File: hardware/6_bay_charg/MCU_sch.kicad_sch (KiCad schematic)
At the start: 21 parts, among them J2 Conn_ARM_SWD_TagConnect_TC203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, Q1 2N7002, U4 TCA9548APWR, U5 STM32L031K6Tx

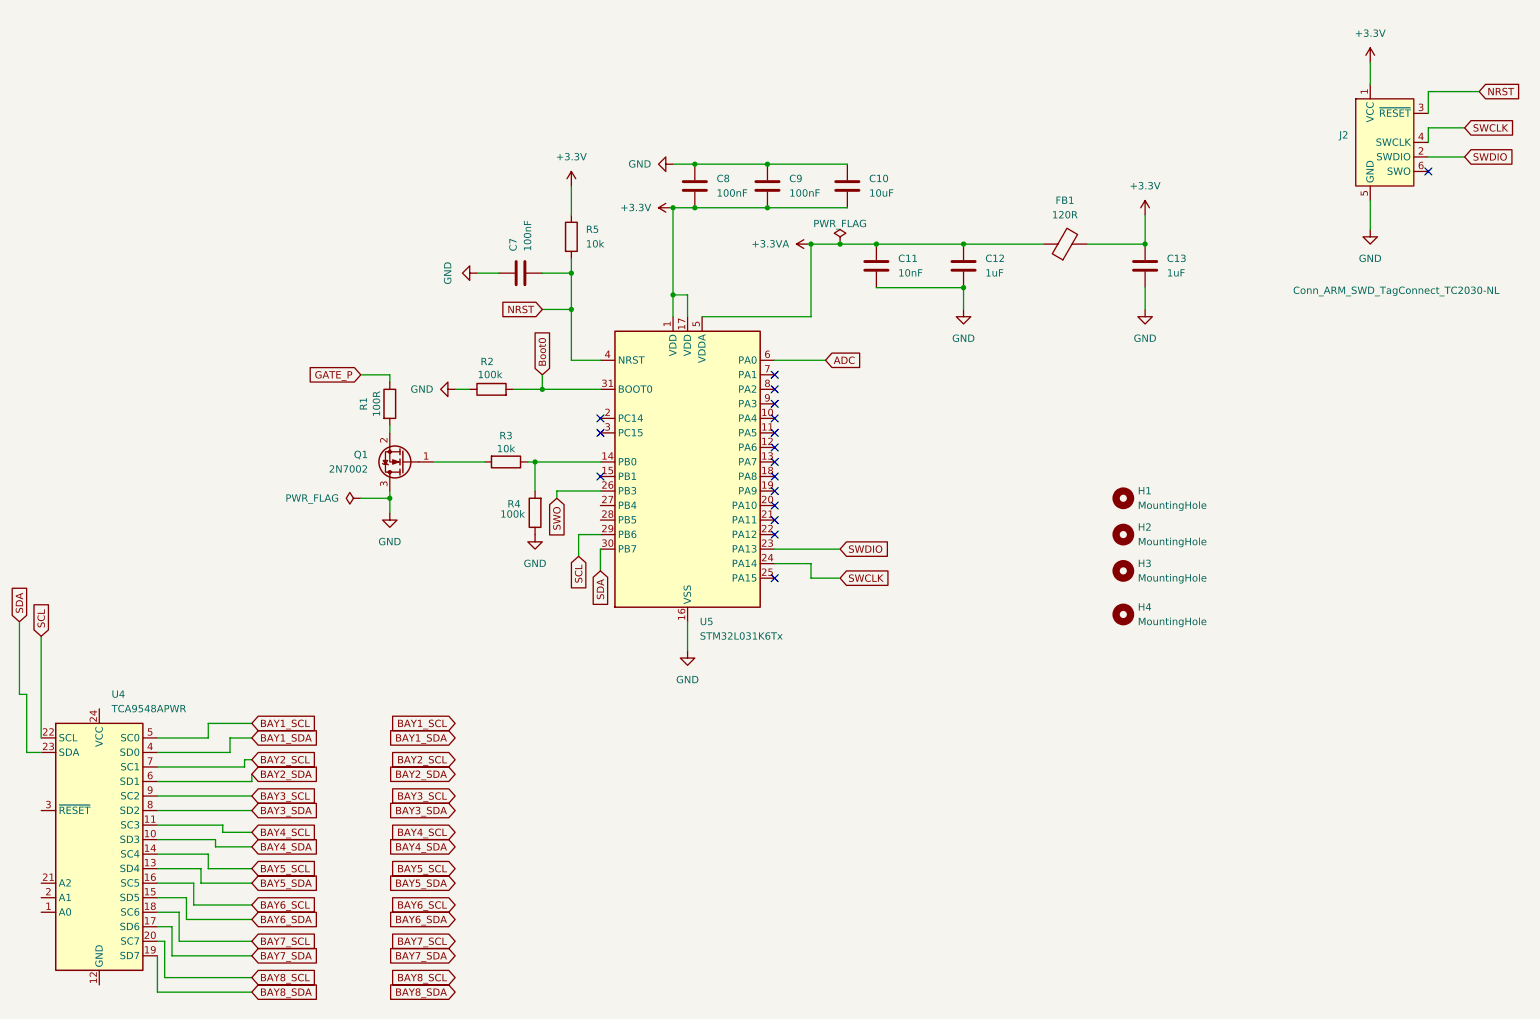
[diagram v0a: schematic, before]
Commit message: adding 3.3v buck sch + bay1
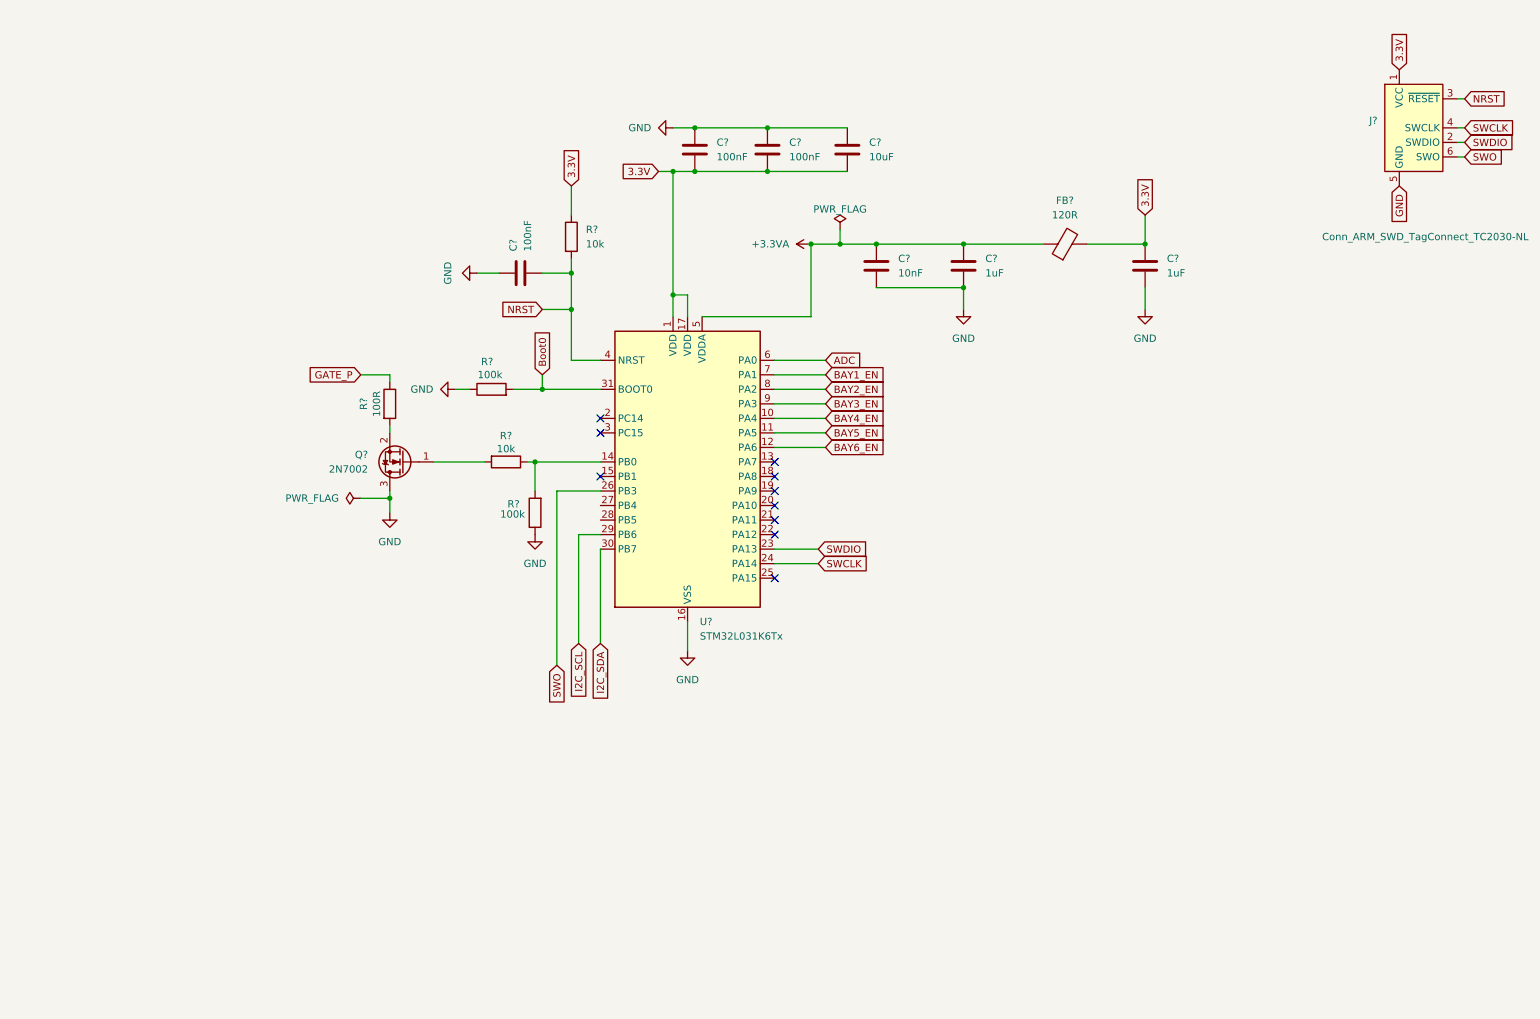
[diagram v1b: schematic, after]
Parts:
- removed H1, H2, H3, H4: MountingHole, MountingHole:MountingHole_2.2mm_M2, symbol Mechanical:MountingHole
- removed U4: TCA9548APWR, Package_SO:TSSOP-24_4.4x7.8mm_P0.65mm, symbol Interface_Expansion:TCA9548APWR
- renumbered C9 to C?, C8 to C?, C11 to C?, C7 to C?, C13 to C?, C12 to C?, C10 to C?, FB1 to FB?, J2 to J?, Q1 to Q?, R3 to R?, R2 to R?, R1 to R?, R4 to R?, R5 to R?, U5 to U?
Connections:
- net SWO: now also J?.6 (SWO)
- net BAY4_EN: now reaches U?.10 (PA4)
- net BAY5_EN: now reaches U?.11 (PA5)
- net BAY6_EN: now reaches U?.12 (PA6)
- net BAY1_EN: now reaches U?.7 (PA1)
- net BAY2_EN: now reaches U?.8 (PA2)
- net BAY3_EN: now reaches U?.9 (PA3)
- net +3.3V renamed 3.3V
- net SCL renamed I2C_SCL
- net SDA renamed I2C_SDA
- no-connect marks 17 -> 10
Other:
- company: (none) -> EOS Positioning Systems
- moved on the sheet: C?, J?

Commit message: Update KiCad schematics: dual GPIO charge/discharge per bay
- Refactored bay power control logic
- Separated GPIOs for charge and discharge paths
- Added safe idle state with hardware interlock
- Improved overall safety and control clarity
- Updated and exported schematic PDF plots
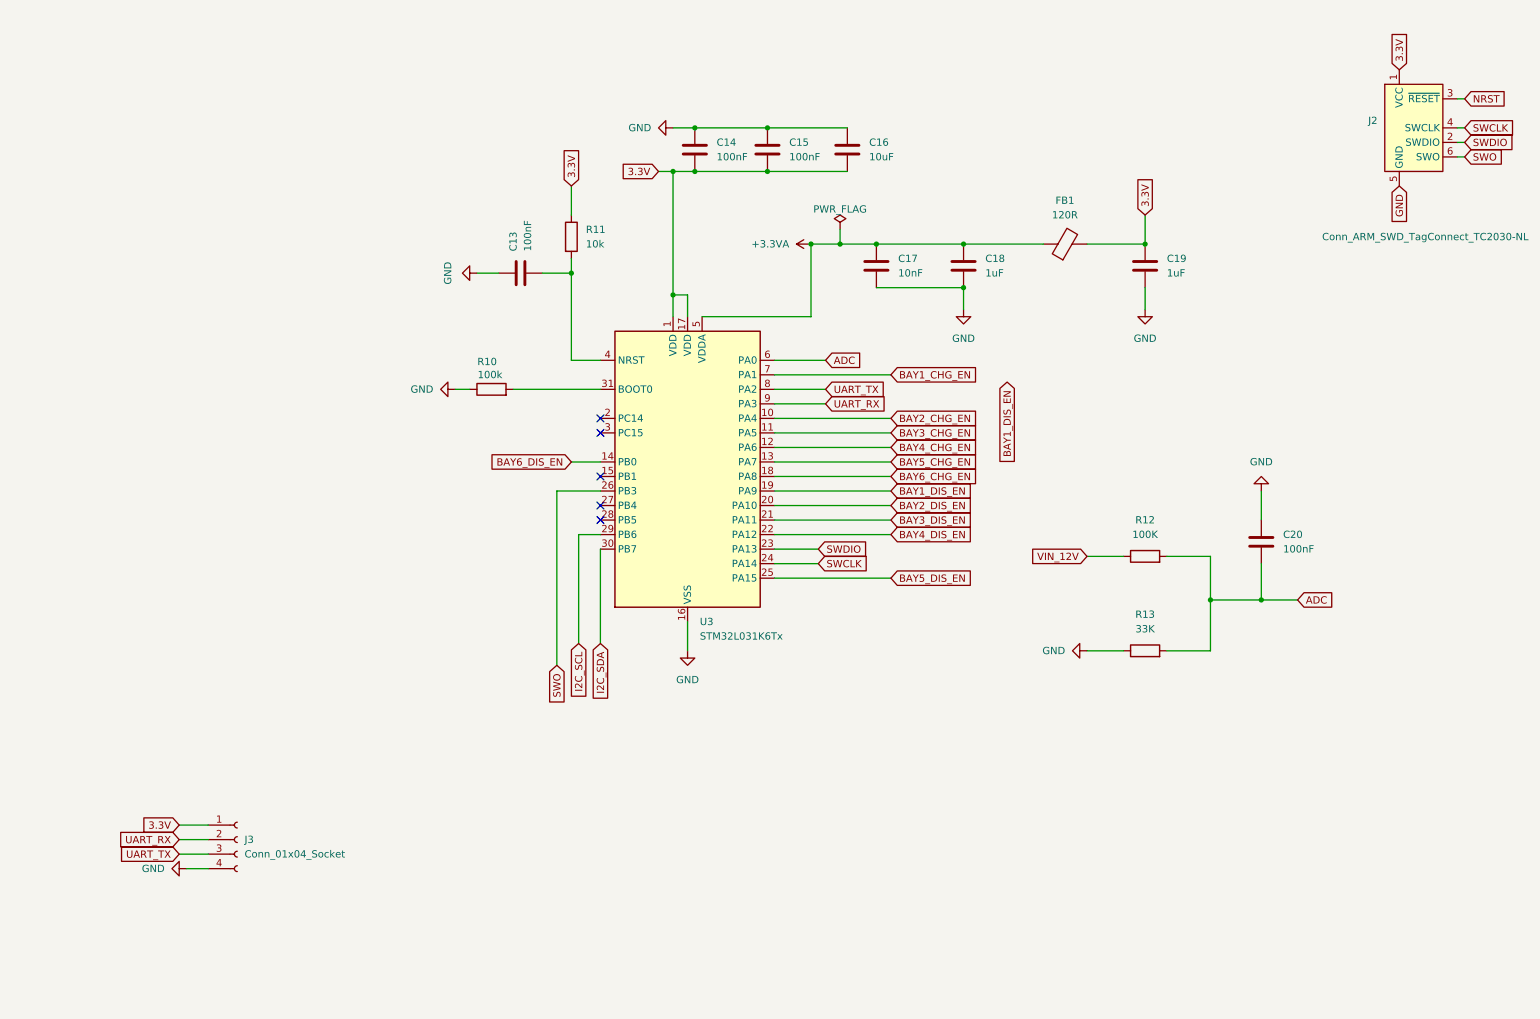
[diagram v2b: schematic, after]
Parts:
- removed Q?: 2N7002, Package_TO_SOT_SMD:SOT-23, symbol Transistor_FET:2N7002
- removed R?: 10k, Resistor_SMD:R_0603_1608Metric, symbol Device:R
- removed R?: 100R, Resistor_SMD:R_0603_1608Metric, symbol Device:R
- removed R?: 100k, Resistor_SMD:R_0603_1608Metric, symbol Device:R
- added C20: 100nF, symbol Device:C
- added J3: Conn_01x04_Socket, Connector_PinSocket_2.54mm:PinSocket_1x04_P2.54mm_Vertical, symbol Connector:Conn_01x04_Socket
- added R12: 100K, symbol Device:R
- added R13: 33K, symbol Device:R
- gave numbers to parts that had none: 12
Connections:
- net 3.3V: now also J3.1 (Pin_1)
- net ADC: now also C20.2, R12.2, R13.2
- net GND: now also C20.1, J3.4 (Pin_4), R13.1
- net NRST: no longer C13.2, R11.2, U3.4 (NRST)
- net BAY6_DIS_EN: now reaches U3.14 (PB0)
- net BAY5_CHG_EN: now reaches U3.13 (PA7)
- net BAY6_CHG_EN: now reaches U3.18 (PA8)
- net BAY1_DIS_EN: now reaches U3.19 (PA9)
- net BAY2_DIS_EN: now reaches U3.20 (PA10)
- net BAY3_DIS_EN: now reaches U3.21 (PA11)
- net BAY4_DIS_EN: now reaches U3.22 (PA12)
- net BAY5_DIS_EN: now reaches U3.25 (PA15)
- net BAY1_EN renamed BAY1_CHG_EN
- net BAY2_EN renamed UART_TX
- net UART_TX: now also J3.3 (Pin_3)
- net BAY3_EN renamed UART_RX
- net UART_RX: now also J3.2 (Pin_2)
- net BAY4_EN renamed BAY2_CHG_EN
- net BAY5_EN renamed BAY3_CHG_EN
- net BAY6_EN renamed BAY4_CHG_EN
- net Boot0: no longer names the net of R10.2, U3.31 (BOOT0)
- new net: C13.2, R11.2, U3.4 (NRST)
- new net VIN_12V: R12.1
- no-connect marks 10 -> 5
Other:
- title: (none) -> MCU

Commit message: Integrate fan, USB interface, firmware, and cleaned KiCad schematics
- Added 12V fan for thermal management
- Integrated USB interface (hardware and firmware)
- Added initial firmware implementation
- Cleaned and refactored KiCad schematics
- Updated and regenerated schematic PDF plots
- Updated project README to reflect latest architecture
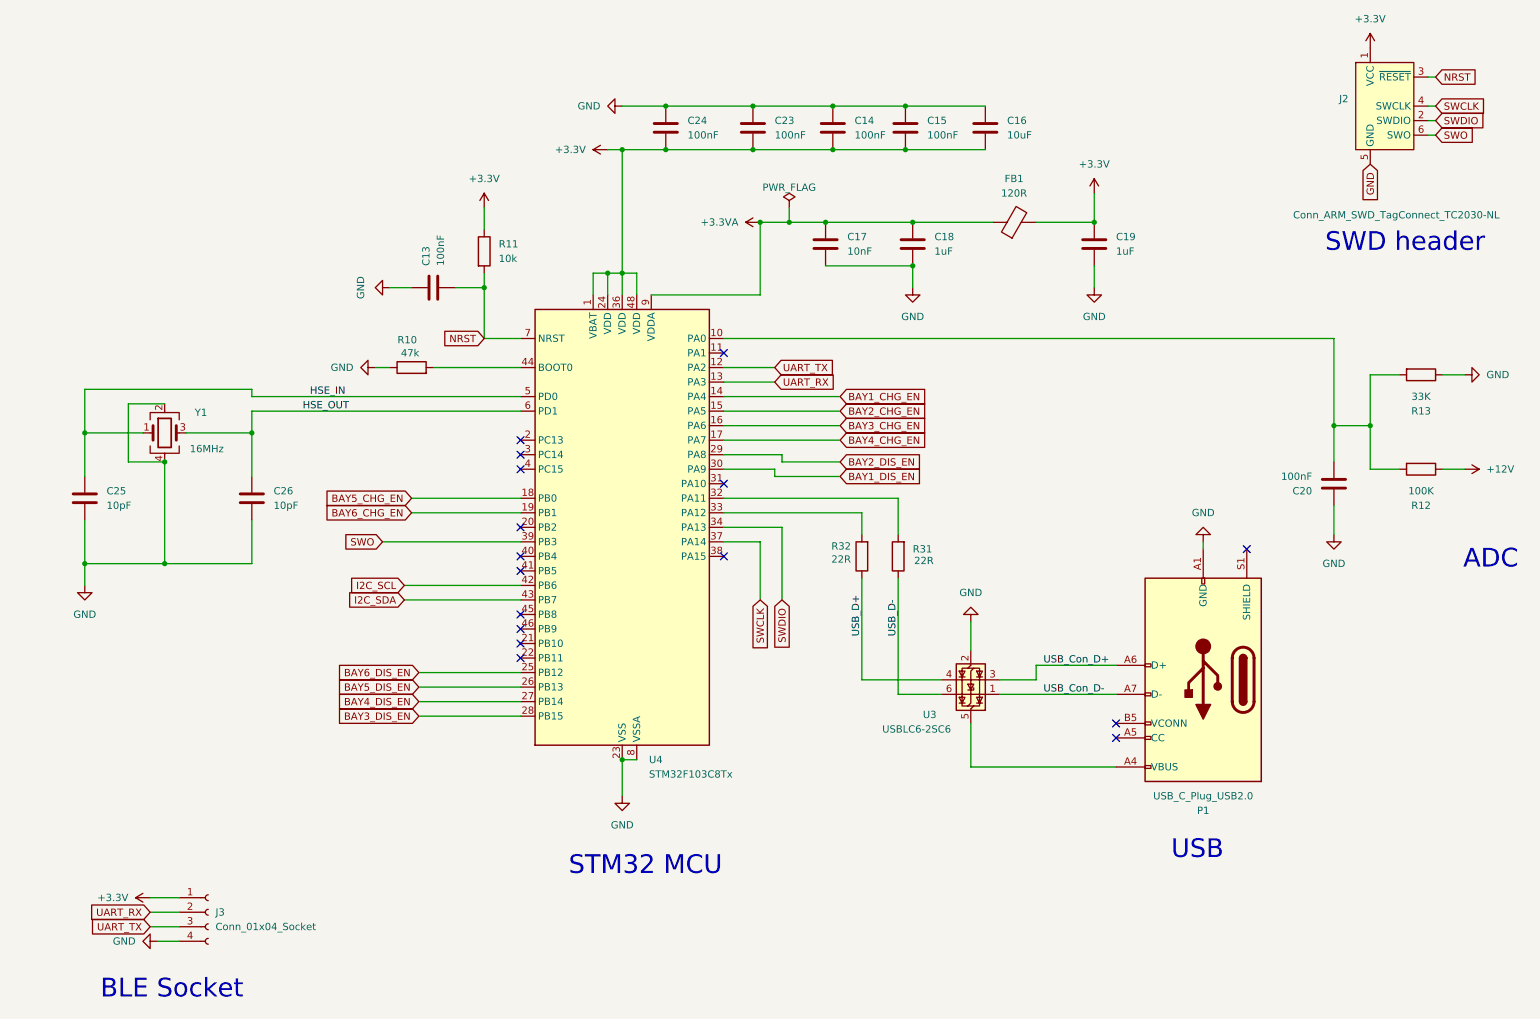
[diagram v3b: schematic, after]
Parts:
- removed U3: STM32L031K6Tx, Package_QFP:LQFP-32_7x7mm_P0.8mm, symbol MCU_ST_STM32L0:STM32L031K6Tx
- added C23, C24: 100nF, Capacitor_SMD:C_0402_1005Metric, symbol Device:C
- added C25, C26: 10pF, symbol Device:C
- added P1: USB_C_Plug_USB2.0, symbol Connector:USB_C_Plug_USB2.0
- added R31, R32: 22R, symbol Device:R
- added U3: USBLC6-2SC6, Package_TO_SOT_SMD:SOT-23-6, symbol Power_Protection:USBLC6-2SC6
- added U4: STM32F103C8Tx, Package_QFP:LQFP-48_7x7mm_P0.5mm, symbol MCU_ST_STM32F1:STM32F103C8Tx
- added Y1: 16MHz, symbol Device:Crystal_GND24
- R10: value 100k -> 47k
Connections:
- net +3.3VA: now also U4.9 (VDDA)
- net BAY1_CHG_EN: now also U4.14 (PA4)
- net BAY1_DIS_EN: now also U4.30 (PA9)
- net BAY2_CHG_EN: now also U4.15 (PA5)
- net BAY2_DIS_EN: now also U4.29 (PA8)
- net BAY3_CHG_EN: now also U4.16 (PA6)
- net BAY3_DIS_EN: now also U4.28 (PB15)
- net BAY4_CHG_EN: now also U4.17 (PA7)
- net BAY4_DIS_EN: now also U4.27 (PB14)
- net BAY5_CHG_EN: now also U4.18 (PB0)
- net BAY5_DIS_EN: now also U4.26 (PB13)
- net BAY6_CHG_EN: now also U4.19 (PB1)
- net BAY6_DIS_EN: now also U4.25 (PB12)
- net GND: now also C23.1, C24.1, C25.2, C26.2, P1.A1 (GND), P1.A12 (GND), P1.B1 (GND), P1.B12 (GND), U3.2 (GND), U4.23 (VSS), U4.35 (VSS), U4.47 (VSS), U4.8 (VSSA), Y1.2, Y1.4
- net I2C_SCL: now also U4.42 (PB6)
- net I2C_SDA: now also U4.43 (PB7)
- net NRST: now also C13.2, R11.2, U4.7 (NRST)
- net SWCLK: now also U4.37 (PA14)
- net SWDIO: now also U4.34 (PA13)
- net SWO: now also U4.39 (PB3)
- net UART_RX: now also U4.13 (PA3)
- net UART_TX: now also U4.12 (PA2)
- net at R10.2: now also U4.44 (BOOT0)
- net 3.3V renamed +3.3V
- net +3.3V: now also C23.2, C24.2, U4.1 (VBAT), U4.24 (VDD), U4.36 (VDD), U4.48 (VDD)
- net ADC: no longer names the net of C20.2, R12.2, R13.2
- net ADC: now also U4.10 (PA0)
- net VIN_12V renamed +12V
- new net: P1.A4 (VBUS), P1.A9 (VBUS), P1.B4 (VBUS), P1.B9 (VBUS), U3.5 (VBUS)
- new net: R31.2, U4.32 (PA11)
- new net: R32.2, U4.33 (PA12)
- new net HSE_IN: C25.1, U4.5 (PD0), Y1.1
- new net HSE_OUT: C26.1, U4.6 (PD1), Y1.3
- new net USB_Con_D+: P1.A6 (D+), U3.3 (I/O2)
- new net USB_Con_D-: P1.A7 (D-), U3.1 (I/O1)
- new net USB_D+: R32.1, U3.4 (I/O2)
- new net USB_D-: R31.1, U3.6 (I/O1)
- no-connect marks 5 -> 16
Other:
- note added: "ADC"
- note added: "BLE Socket"
- note added: "STM32 MCU"
- note added: "SWD header"
- note added: "USB"
- moved on the sheet: C13, C14, C15, C16, C17, C18, C19, C20, FB1, J2, J3, R10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

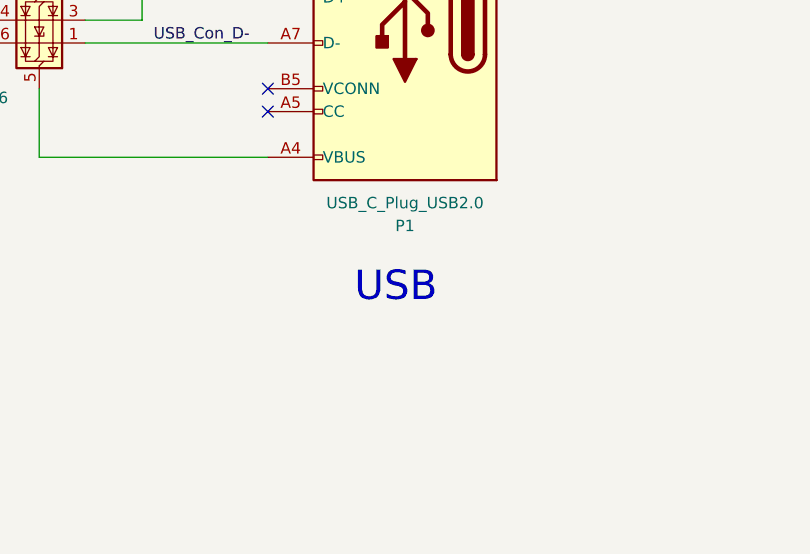
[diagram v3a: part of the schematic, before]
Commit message: updating FSM diagramme
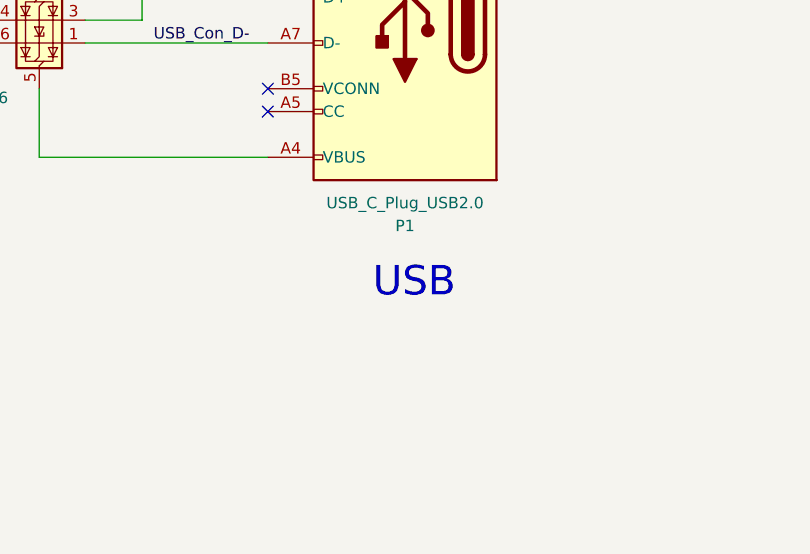
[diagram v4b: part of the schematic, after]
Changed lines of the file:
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@@
 	(text "USB\n"
 		(exclude_from_sim no)
-		(at 221.234 161.798 0)
+		(at 223.266 161.29 0)
 		(effects
 			(font
